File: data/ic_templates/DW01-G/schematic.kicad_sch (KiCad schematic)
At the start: 12 parts, among them J1 B+/B-/P+/P-, Q1 FS8205A, U1 DW01-G

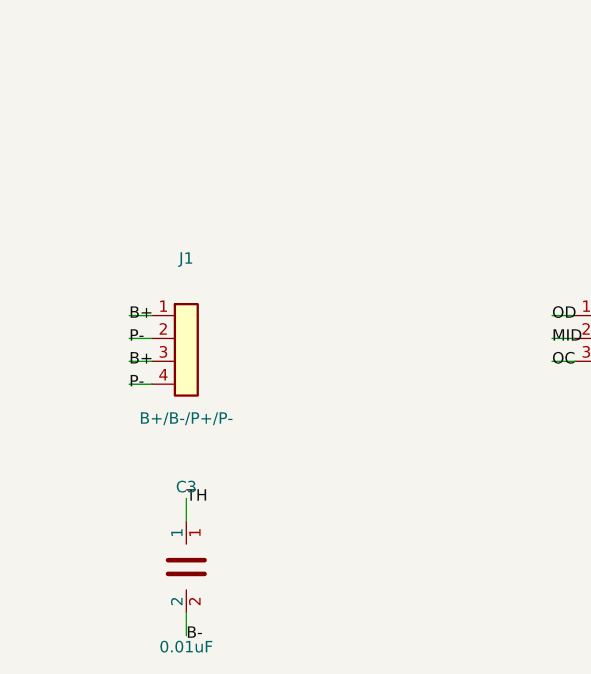
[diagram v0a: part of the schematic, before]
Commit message: fix: 修复黑框检测阈值策略 — 固定阈值70改为 Otsu+Adaptive 混合阈值
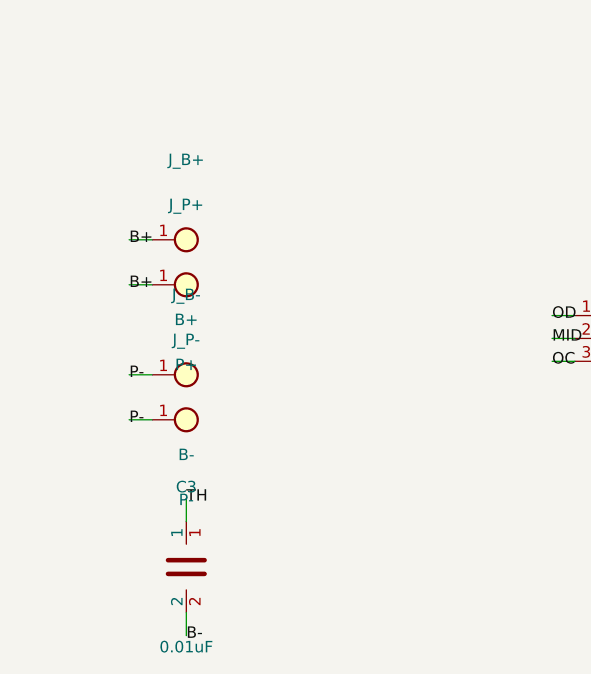
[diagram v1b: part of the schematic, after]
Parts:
- removed J1: B+/B-/P+/P-, Connector_PinHeader_2.54mm:PinHeader_1x04_P2.54mm_Vertical, symbol battery_protection:Conn_01x04
- added J_B+: B+, Connector_PinHeader_2.54mm:PinHeader_1x01_P2.54mm_Vertical, symbol battery_protection:Conn_01x01
- added J_B-: B-, Connector_PinHeader_2.54mm:PinHeader_1x01_P2.54mm_Vertical, symbol battery_protection:Conn_01x01
- added J_P+: P+, Connector_PinHeader_2.54mm:PinHeader_1x01_P2.54mm_Vertical, symbol battery_protection:Conn_01x01
- added J_P-: P-, Connector_PinHeader_2.54mm:PinHeader_1x01_P2.54mm_Vertical, symbol battery_protection:Conn_01x01
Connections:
- net B+: now also J_B+.1, J_P+.1
- net P-: now also J_B-.1, J_P-.1
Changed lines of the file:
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@@
     (comment 1 "Common-port, FS8205A companion")
   )
-  (symbol (lib_id "battery_protection:Conn_01x04") (at 25.4 60.96 0) (unit 1)
-    (exclude_from_sim no) (in_bom yes) (on_board yes) (dnp no)
-    (property "Reference" "J1" (at 25.4 52.07 0)
-      (effects (font (size 1.27 1.27))))
-    (property "Value" "B+/B-/P+/P-" (at 25.4 69.85 0)
-      (effects (font (size 1.27 1.27))))
-    (property "Footprint" "Connector_PinHeader_2.54mm:PinHeader_1x04_P2.54mm_Vertical" (at 0 0 0)
-      (effects (font (size 1.27 1.27)) hide))
-    (property "Datasheet" "" (at 0 0 0)
-      (effects (font (size 1.27 1.27)) hide))
-    (instances
-      (project "template" (path "/64ca2664-9d44-42f3-b461-7f5d2f994412" (reference "J1") (unit 1))))
-    (pin "1")
-    (pin "2")
-    (pin "3")
-    (pin "4")
+  (symbol (lib_id "battery_protection:Conn_01x01") (at 25.4 50.0 0) (unit 1)
+    (exclude_from_sim no) (in_bom yes) (on_board yes) (dnp no)
+    (property "Reference" "J_B+" (at 25.4 41.11 0)
+      (effects (font (size 1.27 1.27))))
+    (property "Value" "B+" (at 25.4 58.89 0)
+      (effects (font (size 1.27 1.27))))
+    (property "Footprint" "Connector_PinHeader_2.54mm:PinHeader_1x01_P2.54mm_Vertical" (at 0 0 0)
+      (effects (font (size 1.27 1.27)) hide))
+    (property "Datasheet" "" (at 0 0 0)
+      (effects (font (size 1.27 1.27)) hide))
+    (instances
+      (project "template" (path "/3b414bfc-e7ac-4c55-be05-818c602a4c56" (reference "J_B+") (unit 1))))
+    (pin "1")
+  )
+  (symbol (lib_id "battery_protection:Conn_01x01") (at 25.4 55.0 0) (unit 1)
+    (exclude_from_sim no) (in_bom yes) (on_board yes) (dnp no)
+    (property "Reference" "J_P+" (at 25.4 46.11 0)
+      (effects (font (size 1.27 1.27))))
+    (property "Value" "P+" (at 25.4 63.89 0)
+      (effects (font (size 1.27 1.27))))
+    (property "Footprint" "Connector_PinHeader_2.54mm:PinHeader_1x01_P2.54mm_Vertical" (at 0 0 0)
+      (effects (font (size 1.27 1.27)) hide))
+    (property "Datasheet" "" (at 0 0 0)
+      (effects (font (size 1.27 1.27)) hide))
+    (instances
+      (project "template" (path "/cd23afd3-b44f-4554-9ad3-a907889ac409" (reference "J_P+") (unit 1))))
+    (pin "1")
+  )
+  (symbol (lib_id "battery_protection:Conn_01x01") (at 25.4 65.0 0) (unit 1)
+    (exclude_from_sim no) (in_bom yes) (on_board yes) (dnp no)
+    (property "Reference" "J_B-" (at 25.4 56.11 0)
+      (effects (font (size 1.27 1.27))))
+    (property "Value" "B-" (at 25.4 73.89 0)
+      (effects (font (size 1.27 1.27))))
+    (property "Footprint" "Connector_PinHeader_2.54mm:PinHeader_1x01_P2.54mm_Vertical" (at 0 0 0)
+      (effects (font (size 1.27 1.27)) hide))
+    (property "Datasheet" "" (at 0 0 0)
+      (effects (font (size 1.27 1.27)) hide))
+    (instances
+      (project "template" (path "/c78b7ef4-2002-4e3d-81cb-c4f14f2fee51" (reference "J_B-") (unit 1))))
+    (pin "1")
+  )
+  (symbol (lib_id "battery_protection:Conn_01x01") (at 25.4 70.0 0) (unit 1)
+    (exclude_from_sim no) (in_bom yes) (on_board yes) (dnp no)
+    (property "Reference" "J_P-" (at 25.4 61.11 0)
+      (effects (font (size 1.27 1.27))))
+    (property "Value" "P-" (at 25.4 78.89 0)
+      (effects (font (size 1.27 1.27))))
+    (property "Footprint" "Connector_PinHeader_2.54mm:PinHeader_1x01_P2.54mm_Vertical" (at 0 0 0)
+      (effects (font (size 1.27 1.27)) hide))
+    (property "Datasheet" "" (at 0 0 0)
+      (effects (font (size 1.27 1.27)) hide))
+    (instances
+      (project "template" (path "/0e360480-9272-4de9-a114-c8ff22c205d0" (reference "J_P-") (unit 1))))
+    (pin "1")
   )
   (symbol (lib_id "battery_protection:DW01-G") (at 76.2 60.96 0) (unit 1)
@@
       (effects (font (size 1.27 1.27)) hide))
     (instances
-      (project "template" (path "/453c17ab-ecd2-467e-b19a-f9f14386cb78" (reference "U1") (unit 1))))
+      (project "template" (path "/3fbe03d7-25a3-48b4-a8ec-8e2745d8c246" (reference "U1") (unit 1))))
     (pin "1")
     (pin "2")
@@
       (effects (font (size 1.27 1.27)) hide))
     (instances
-      (project "template" (path "/a62f3887-a20a-4021-aa8d-60eb071aa717" (reference "Q1") (unit 1))))
+      (project "template" (path "/e6698ed5-de6e-41c7-856d-4adc0dfa7262" (reference "Q1") (unit 1))))
     (pin "1")
     (pin "2")
@@
       (effects (font (size 1.27 1.27)) hide))
     (instances
-      (project "template" (path "/2a49669a-6888-47e9-a25e-742eb30fe753" (reference "R1") (unit 1))))
+      (project "template" (path "/b236fd10-5b2a-4675-a82b-0cf4218ef0f7" (reference "R1") (unit 1))))
     (pin "1")
     (pin "2")
@@
       (effects (font (size 1.27 1.27)) hide))
     (instances
-      (project "template" (path "/e4d78243-6c35-4314-a4e1-0098fc06cba3" (reference "R2") (unit 1))))
+      (project "template" (path "/a5f2ee65-9e7b-4836-a3ad-52ff9ca29acf" (reference "R2") (unit 1))))
     (pin "1")
     (pin "2")
@@
       (effects (font (size 1.27 1.27)) hide))
     (instances
-      (project "template" (path "/f5db3458-0770-45d3-aad6-7b3cddb20624" (reference "R3") (unit 1))))
+      (project "template" (path "/cb53713f-a5b3-4b97-a5c0-e8b75eab761f" (reference "R3") (unit 1))))
     (pin "1")
     (pin "2")
@@
       (effects (font (size 1.27 1.27)) hide))
     (instances
-      (project "template" (path "/086c0adc-5338-4b4b-8225-4338dfb7c6a7" (reference "R4") (unit 1))))
+      (project "template" (path "/33920a54-cc6b-4b24-ac71-b18b36b71191" (reference "R4") (unit 1))))
     (pin "1")
     (pin "2")
@@
       (effects (font (size 1.27 1.27)) hide))
     (instances
-      (project "template" (path "/1b851e48-e526-4b4c-af9f-3922d970dba9" (reference "C1") (unit 1))))
+      (project "template" (path "/cf652060-5ccc-4bfd-8599-1d5603016665" (reference "C1") (unit 1))))
     (pin "1")
     (pin "2")
@@
       (effects (font (size 1.27 1.27)) hide))
     (instances
-      (project "template" (path "/2f80b5e8-9580-43bb-99cf-bbb14c0502ed" (reference "C2") (unit 1))))
+      (project "template" (path "/83063f93-bc5e-4c98-8dfe-dbdeb7d4bb05" (reference "C2") (unit 1))))
     (pin "1")
     (pin "2")
@@
       (effects (font (size 1.27 1.27)) hide))
     (instances
-      (project "template" (path "/8bfb3eda-36d5-452e-bd85-8aea324a2193" (reference "C3") (unit 1))))
+      (project "template" (path "/0badacd8-5fa7-4ad1-88bb-5541b2be1f5a" (reference "C3") (unit 1))))
     (pin "1")
     (pin "2")
@@
       (effects (font (size 1.27 1.27)) hide))
     (instances
-      (project "template" (path "/51bfa4ed-8ca7-409c-a9d0-832a913fdca2" (reference "TP_TH") (unit 1))))
+      (project "template" (path "/1688bc6b-6600-42d9-924f-f1cd6dab5088" (reference "TP_TH") (unit 1))))
     (pin "1")
   )
@@
       (effects (font (size 1.27 1.27)) hide))
     (instances
-      (project "template" (path "/1972cfc2-29cb-4b2f-a0a9-0dfccddefdb0" (reference "TP_ID") (unit 1))))
-    (pin "1")
-  )
-  (wire (pts (xy 21.59 58.42) (xy 19.05 58.42))
-    (stroke (width 0) (type default))
-)
-  (label "B+" (at 19.05 58.42 0) (fields_autoplaced yes)
-    (effects (font (size 1.27 1.27)) (justify left))
-)
-  (wire (pts (xy 21.59 60.96) (xy 19.05 60.96))
-    (stroke (width 0) (type default))
-)
-  (label "P-" (at 19.05 60.96 0) (fields_autoplaced yes)
-    (effects (font (size 1.27 1.27)) (justify left))
-)
-  (wire (pts (xy 21.59 63.5) (xy 19.05 63.5))
-    (stroke (width 0) (type default))
-)
-  (label "B+" (at 19.05 63.5 0) (fields_autoplaced yes)
-    (effects (font (size 1.27 1.27)) (justify left))
-)
-  (wire (pts (xy 21.59 66.04) (xy 19.05 66.04))
-    (stroke (width 0) (type default))
-)
-  (label "P-" (at 19.05 66.04 0) (fields_autoplaced yes)
-    (effects (font (size 1.27 1.27)) (justify left))
-)
+      (project "template" (path "/bdbb5b50-1cb3-45ee-aac1-d4bc3224ce37" (reference "TP_ID") (unit 1))))
+    (pin "1")
+  )
+  (wire (pts (xy 21.59 50.0) (xy 19.05 50.0))
+    (stroke (width 0) (type default))
+)
+  (label "B+" (at 19.05 50.0 0) (fields_autoplaced yes)
+    (effects (font (size 1.27 1.27)) (justify left))
+)
+  (wire (pts (xy 21.59 55.0) (xy 19.05 55.0))
+    (stroke (width 0) (type default))
+)
+  (label "B+" (at 19.05 55.0 0) (fields_autoplaced yes)
+    (effects (font (size 1.27 1.27)) (justify left))
+)
+  (wire (pts (xy 21.59 65.0) (xy 19.05 65.0))
+    (stroke (width 0) (type default))
+)
+  (label "P-" (at 19.05 65.0 0) (fields_autoplaced yes)
+    (effects (font (size 1.27 1.27)) (justify left))
+)
+  (wire (pts (xy 21.59 70.0) (xy 19.05 70.0))
+    (stroke (width 0) (type default))
+)
+  (label "P-" (at 19.05 70.0 0) (fields_autoplaced yes)
+    (effects (font (size 1.27 1.27)) (justify left))
+)
